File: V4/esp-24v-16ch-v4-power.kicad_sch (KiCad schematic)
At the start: 37 parts, among them J5 VIN, J6 USB_C_Receptacle_USB2.0, Q1 WPM2015-3/TR, Q2 MMUN2211LT3G, U1 SY8089A1AAC, U2 TX4138

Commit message: Revising the schematics
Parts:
- R2, R3: value 5,1k/62,5mW -> 5,1k
- R8: value 10k/62,5mW -> 10k
- R9: value 1k/62,5mW -> 1k
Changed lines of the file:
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@@
 			)
 		)
-		(property "Value" "5,1k/62,5mW"
+		(property "Value" "5,1k"
 			(at 80.01 99.06 0)
 			(effects
@@
 			)
 		)
-		(property "Value" "10k/62,5mW"
+		(property "Value" "10k"
 			(at 182.88 125.095 0)
 			(effects
@@
 			)
 		)
-		(property "Value" "5,1k/62,5mW"
+		(property "Value" "5,1k"
 			(at 99.06 99.06 0)
 			(effects
@@
 			)
 		)
-		(property "Value" "1k/62,5mW"
+		(property "Value" "1k"
 			(at 200.66 144.78 0)
 			(effects

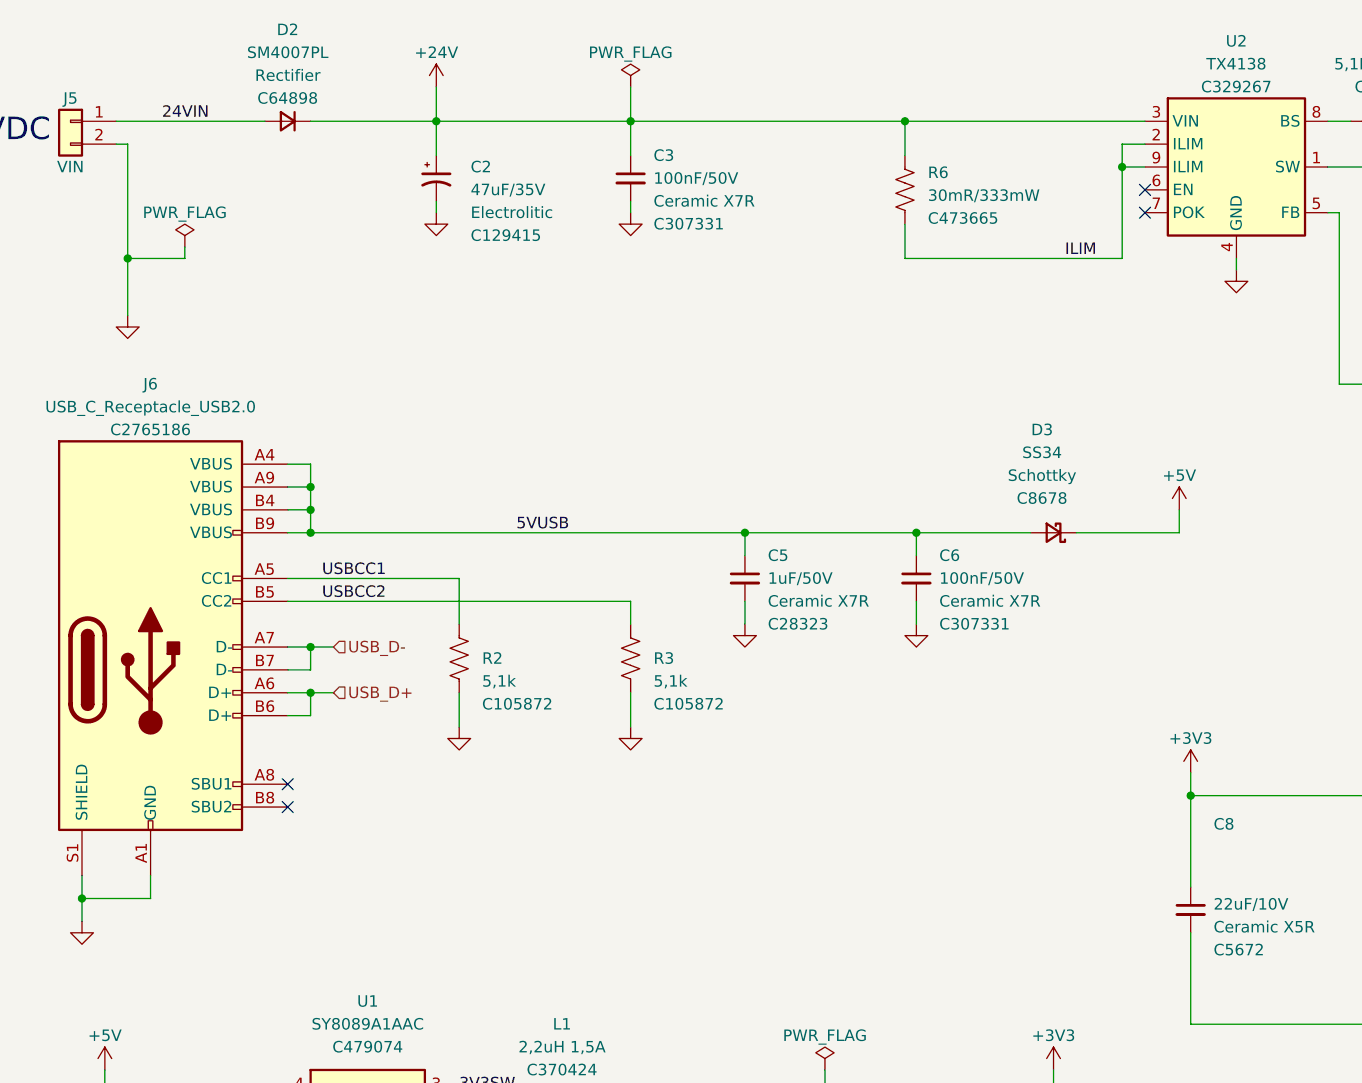
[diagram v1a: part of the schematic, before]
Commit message: Rerouting
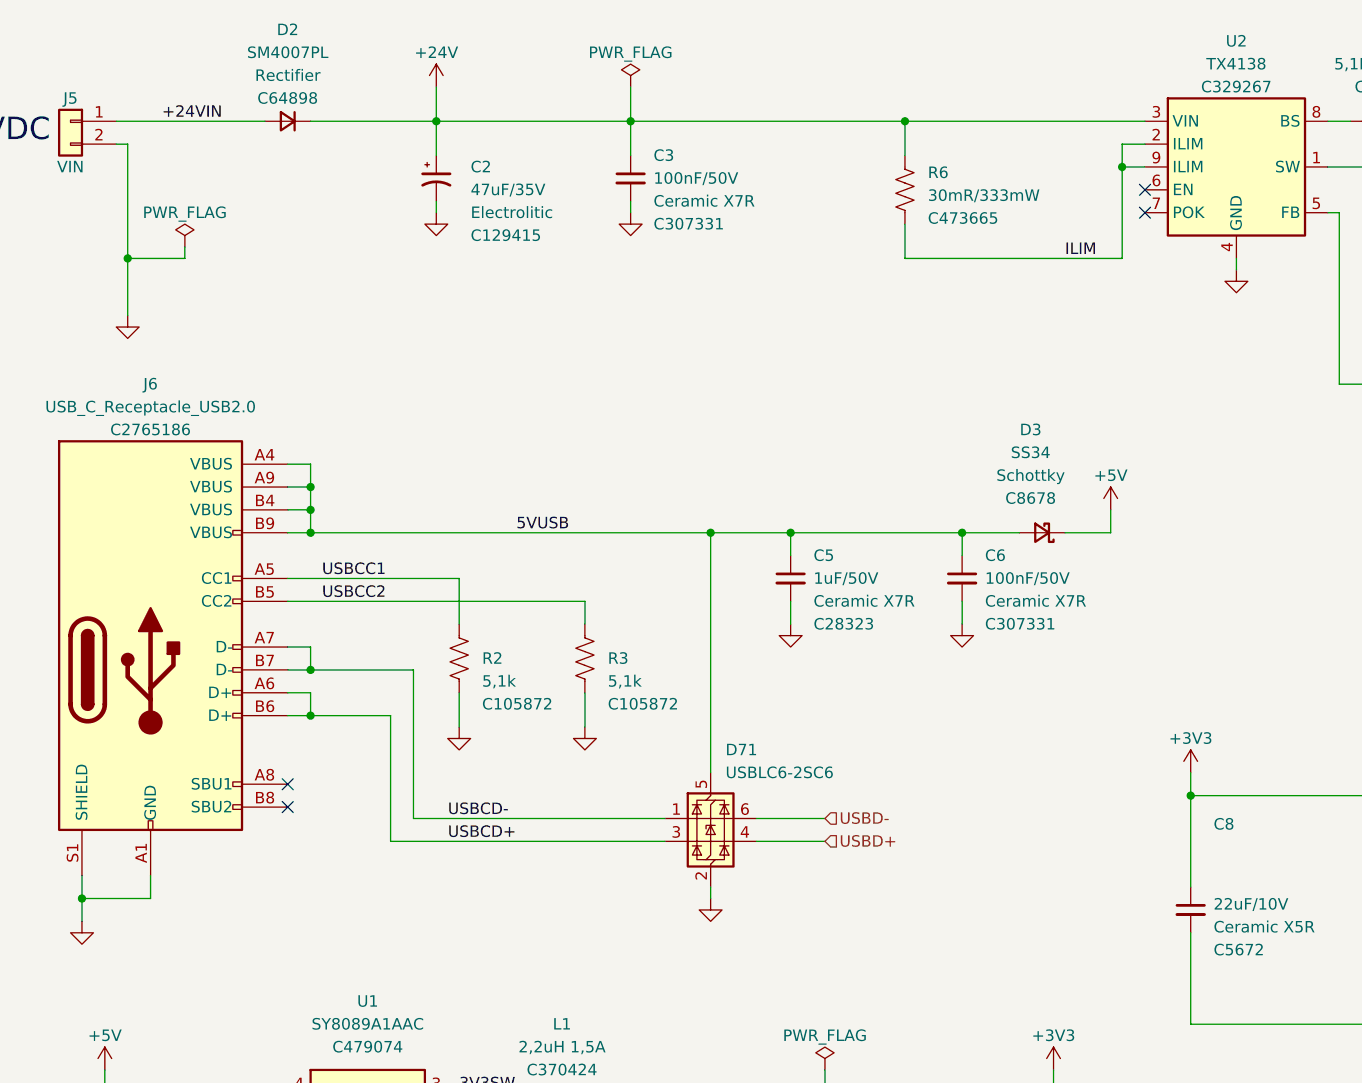
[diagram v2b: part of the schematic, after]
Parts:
- added D71: USBLC6-2SC6, Package_TO_SOT_SMD:SOT-23-6, symbol Power_Protection:USBLC6-2SC6
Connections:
- net 5VUSB: now also D71.5 (VBUS)
- net GND: now also D71.2 (GND)
- net 24VIN renamed +24VIN
- net USB_D+ renamed USBCD+
- net USBCD+: now also D71.3 (I/O2)
- net USB_D- renamed USBCD-
- net USBCD-: now also D71.1 (I/O1)
- new net USBD+: D71.4 (I/O2)
- new net USBD-: D71.6 (I/O1)
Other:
- moved on the sheet: C5, C6, D3, R3

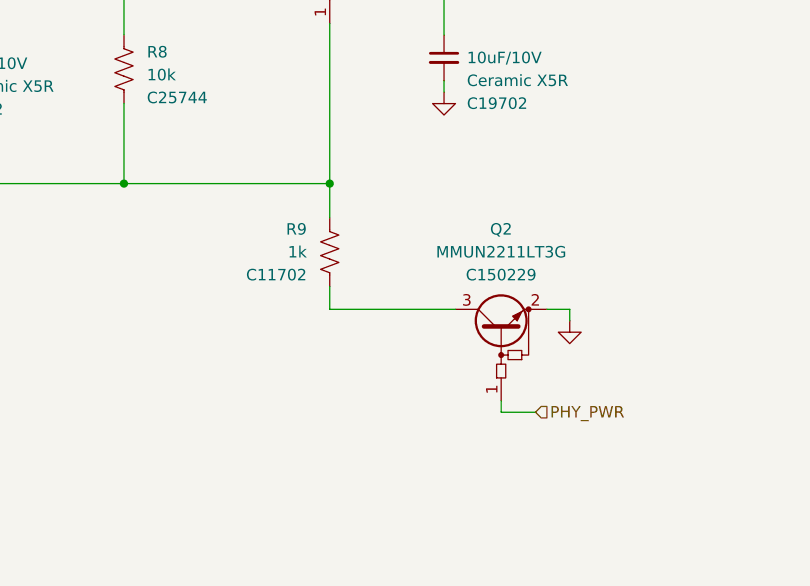
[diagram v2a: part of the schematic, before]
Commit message: Rerouting
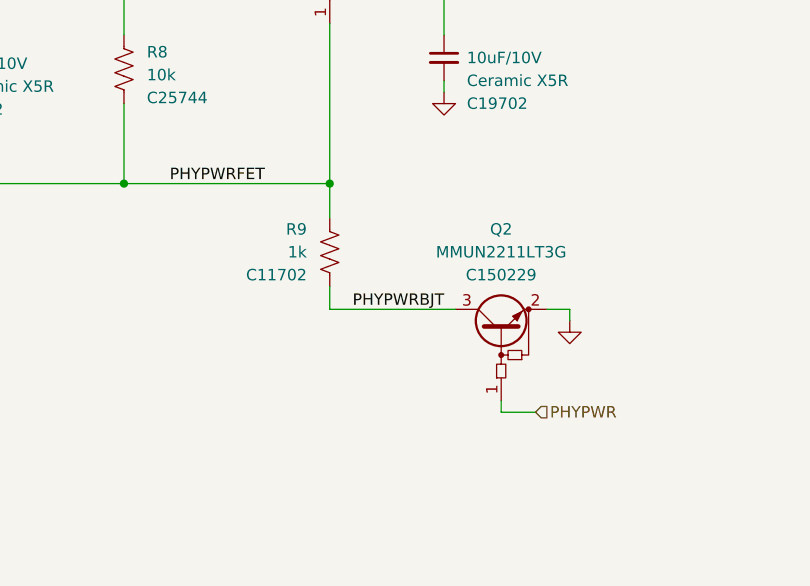
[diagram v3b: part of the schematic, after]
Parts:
- J6: footprint Tales:USB_C_Receptacle_GCT_USB4105-xx-A_16P_TopMnt_Horizontal -> Tales:USB_C_Receptacle_JAE_DX07S024WJ1R350
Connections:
- net PHYPWRFET: now reaches C8.2, Q1.1 (G), R8.2, R9.2
- net PHYPWRBJT: now reaches Q2.3 (C), R9.1
- net PHY_PWR renamed PHYPWR
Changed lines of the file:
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@@
 		)
 	)
+	(label "PHYPWRFET"
+		(at 185.42 137.16 0)
+		(effects
+			(font
+				(size 1.27 1.27)
+			)
+			(justify left bottom)
+		)
+	)
 	(label "5VREF"
 		(at 194.31 66.04 0)
@@
 		)
 	)
+	(label "PHYPWRBJT"
+		(at 205.74 151.13 0)
+		(effects
+			(font
+				(size 1.27 1.27)
+			)
+			(justify left bottom)
+		)
+	)
 	(label "3V3SW"
 		(at 77.47 144.78 0)
@@
 		)
 	)
-	(hierarchical_label "PHY_PWR"
+	(hierarchical_label "PHYPWR"
 		(shape input)
 		(at 226.06 162.56 0)
@@
 		(on_board yes)
 		(dnp no)
-		(fields_autoplaced yes)
 		(property "Reference" "D71"
 			(at 107.0611 106.68 0)
@@
 			)
 		)
-		(property "Footprint" "Tales:USB_C_Receptacle_GCT_USB4105-xx-A_16P_TopMnt_Horizontal"
+		(property "Footprint" "Tales:USB_C_Receptacle_JAE_DX07S024WJ1R350"
 			(at 46.99 92.71 0)
 			(effects

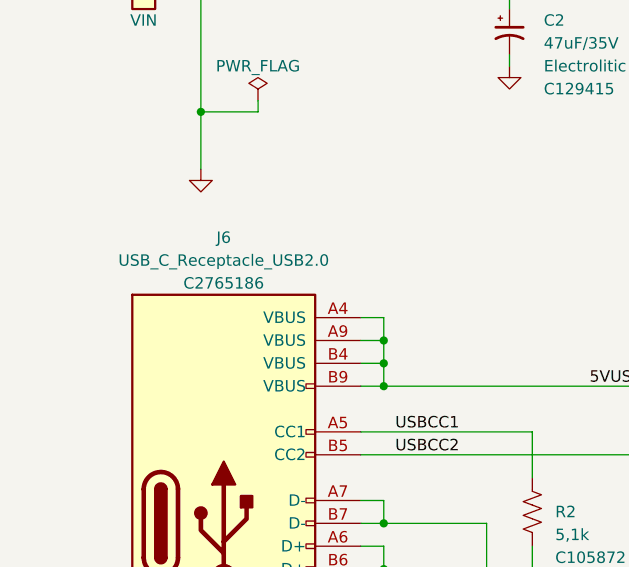
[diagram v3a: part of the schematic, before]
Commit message: Rerouting
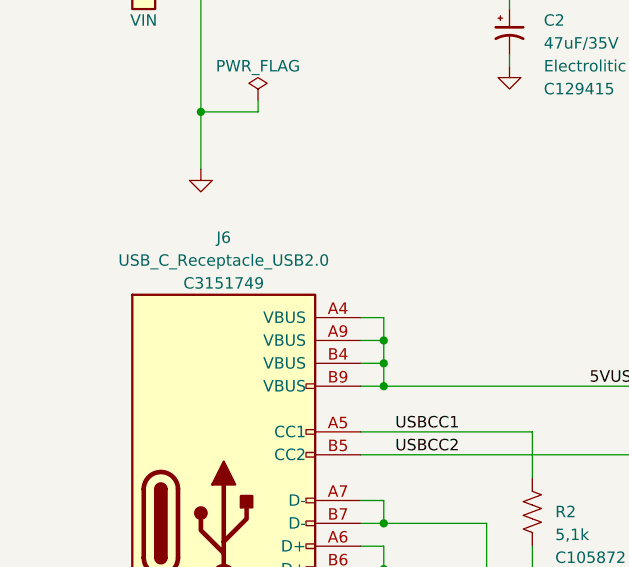
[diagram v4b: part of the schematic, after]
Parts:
- J6: footprint Tales:USB_C_Receptacle_JAE_DX07S024WJ1R350 -> Tales:USB_C_Receptacle_GCT_USB4115-03-C; LCSC Part # C2765186 -> C3151749; Mfr PN TYPE-C 16PIN 2MD(073) -> TYPE-C 16PLT-H10.0; Vendor PN C2765186 -> C3151749
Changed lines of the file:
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@@
 			)
 		)
-		(property "Footprint" "Tales:USB_C_Receptacle_JAE_DX07S024WJ1R350"
+		(property "Footprint" "Tales:USB_C_Receptacle_GCT_USB4115-03-C"
 			(at 46.99 92.71 0)
 			(effects
@@
 			)
 		)
-		(property "LCSC Part #" "C2765186"
+		(property "LCSC Part #" "C3151749"
 			(at 43.18 71.12 0)
 			(effects
@@
 			)
 		)
-		(property "Mfr PN" "TYPE-C 16PIN 2MD(073)"
+		(property "Mfr PN" "TYPE-C 16PLT-H10.0"
 			(at 43.18 92.71 0)
 			(effects
@@
 			)
 		)
-		(property "Vendor PN" "C2765186"
+		(property "Vendor PN" "C3151749"
 			(at 43.18 92.71 0)
 			(effects

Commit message: Rerouting
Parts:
- J6: footprint Tales:USB_C_Receptacle_GCT_USB4115-03-C -> Tales:USB_C_Receptacle_ShouHan_TYPE-C-16PLT-H10.0
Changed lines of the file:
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@@
 			)
 		)
-		(property "Footprint" "Tales:USB_C_Receptacle_GCT_USB4115-03-C"
+		(property "Footprint" "Tales:USB_C_Receptacle_ShouHan_TYPE-C-16PLT-H10.0"
 			(at 46.99 92.71 0)
 			(effects

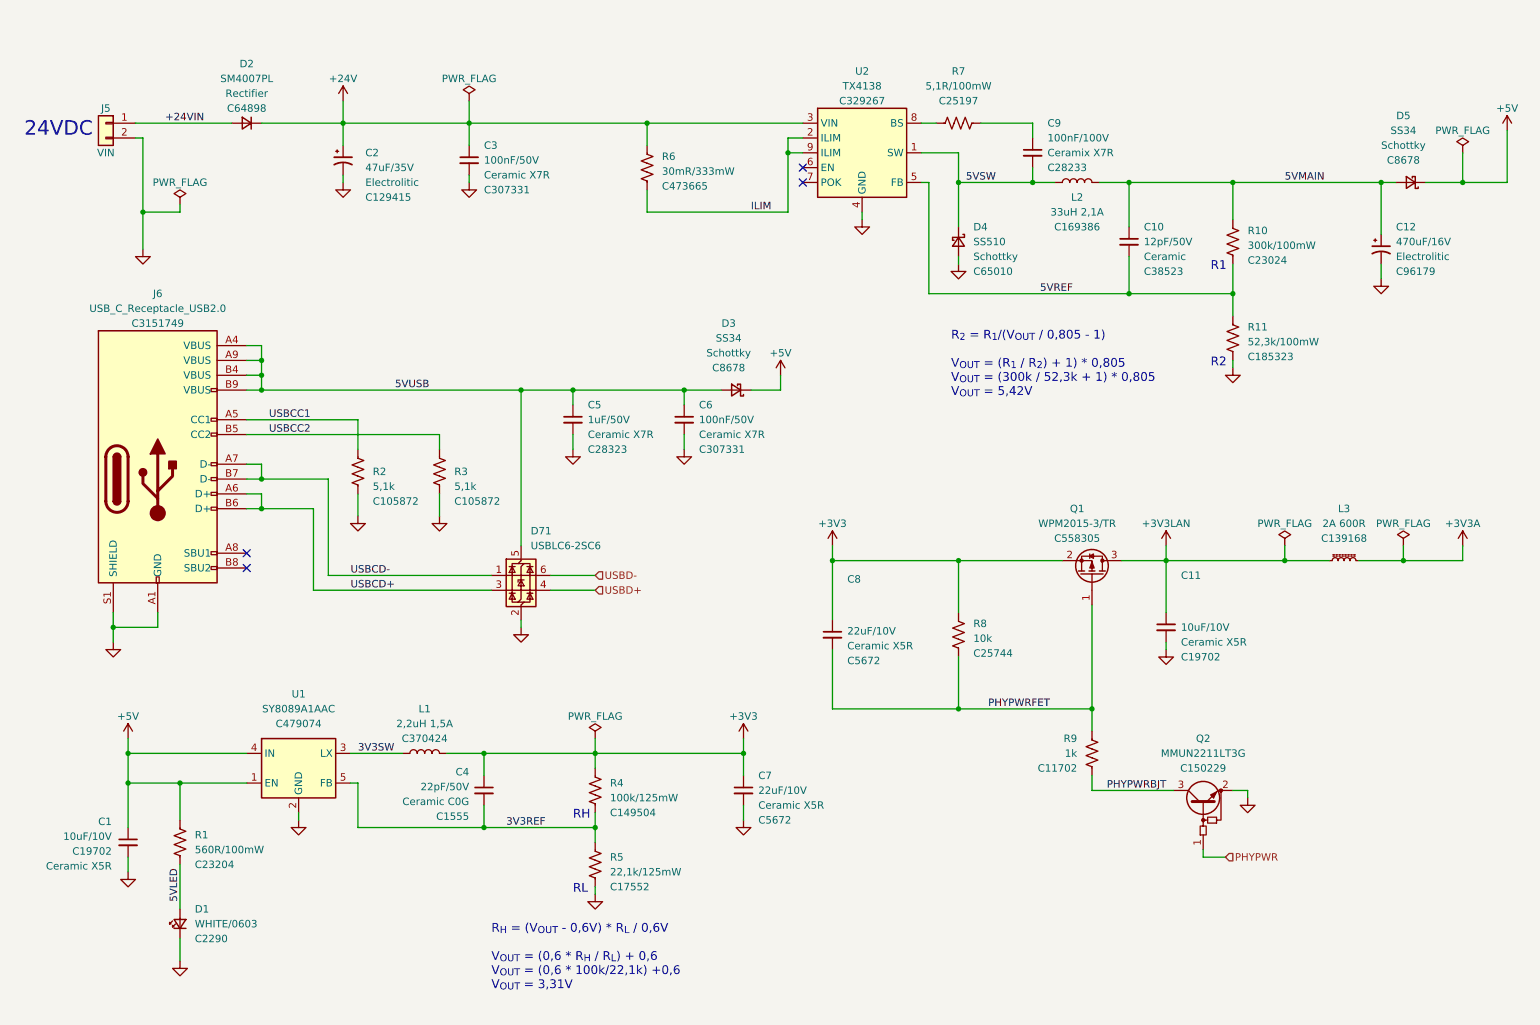
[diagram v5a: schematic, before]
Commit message: Rerouting
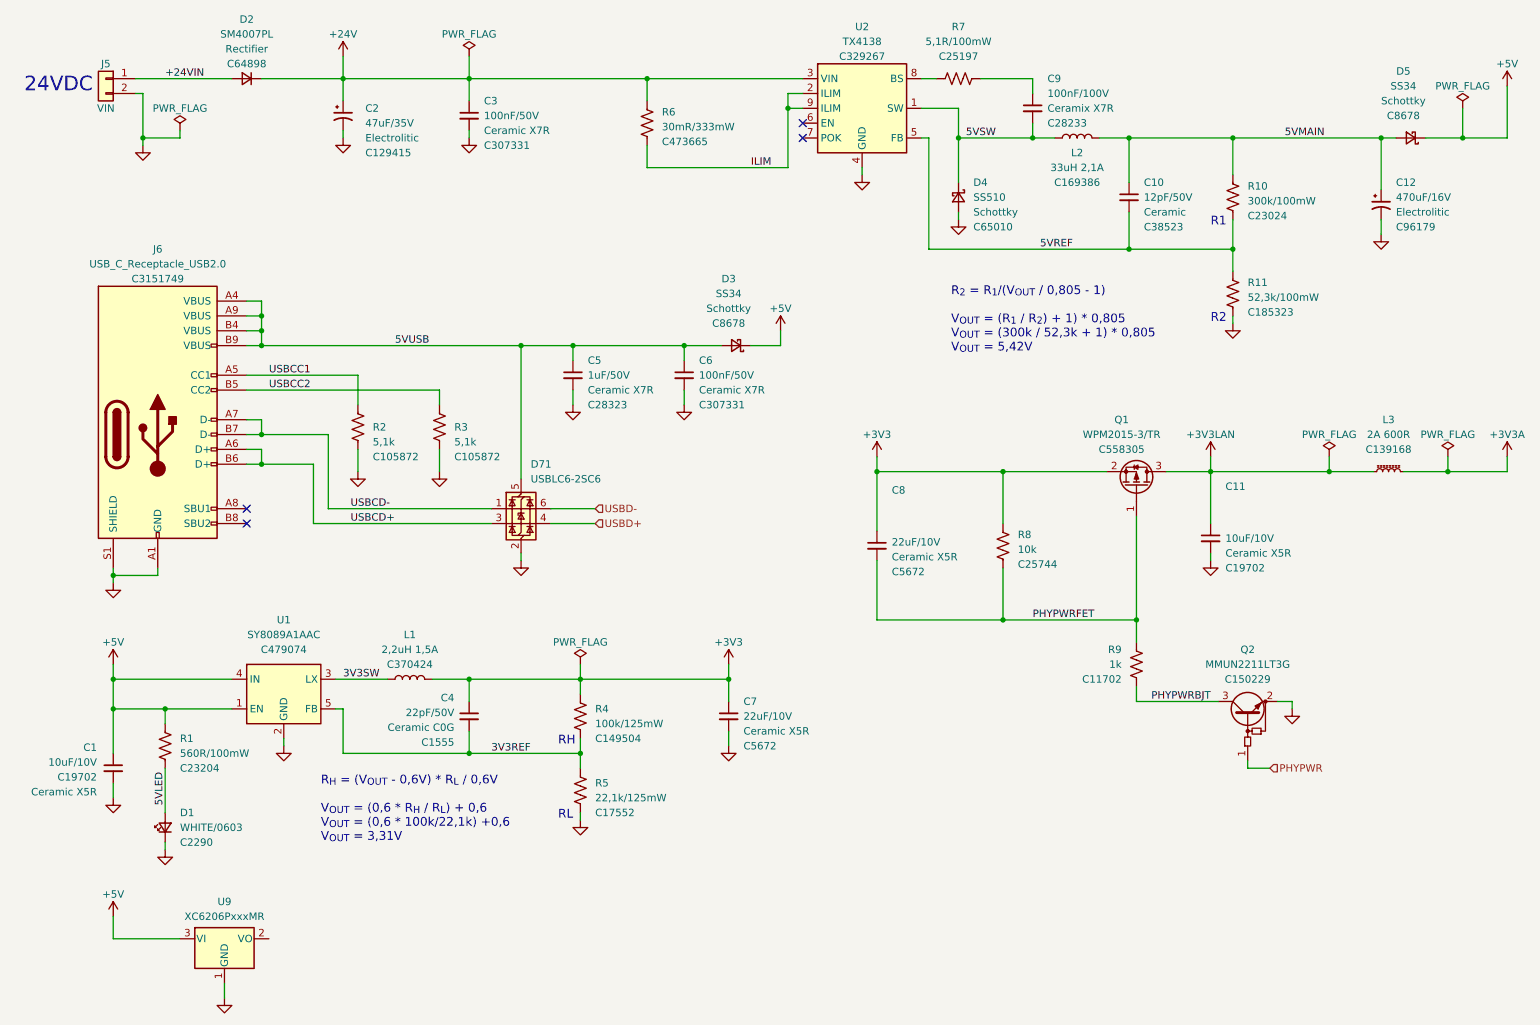
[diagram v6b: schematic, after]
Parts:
- added U9: XC6206PxxxMR, Package_TO_SOT_SMD:SOT-23-3, symbol Regulator_Linear:XC6206PxxxMR
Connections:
- net +5V: now also U9.3 (VI)
- net GND: now also U9.1 (GND)
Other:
- moved on the sheet: C1, C10, C11, C12, C2, C3, C4, C5, C6, C7, C8, C9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
